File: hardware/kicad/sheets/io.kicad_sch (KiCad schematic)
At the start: 22 parts, among them J10 AUX, J11 INPUTS, Q2 AO3400A, U6 ULN2003A

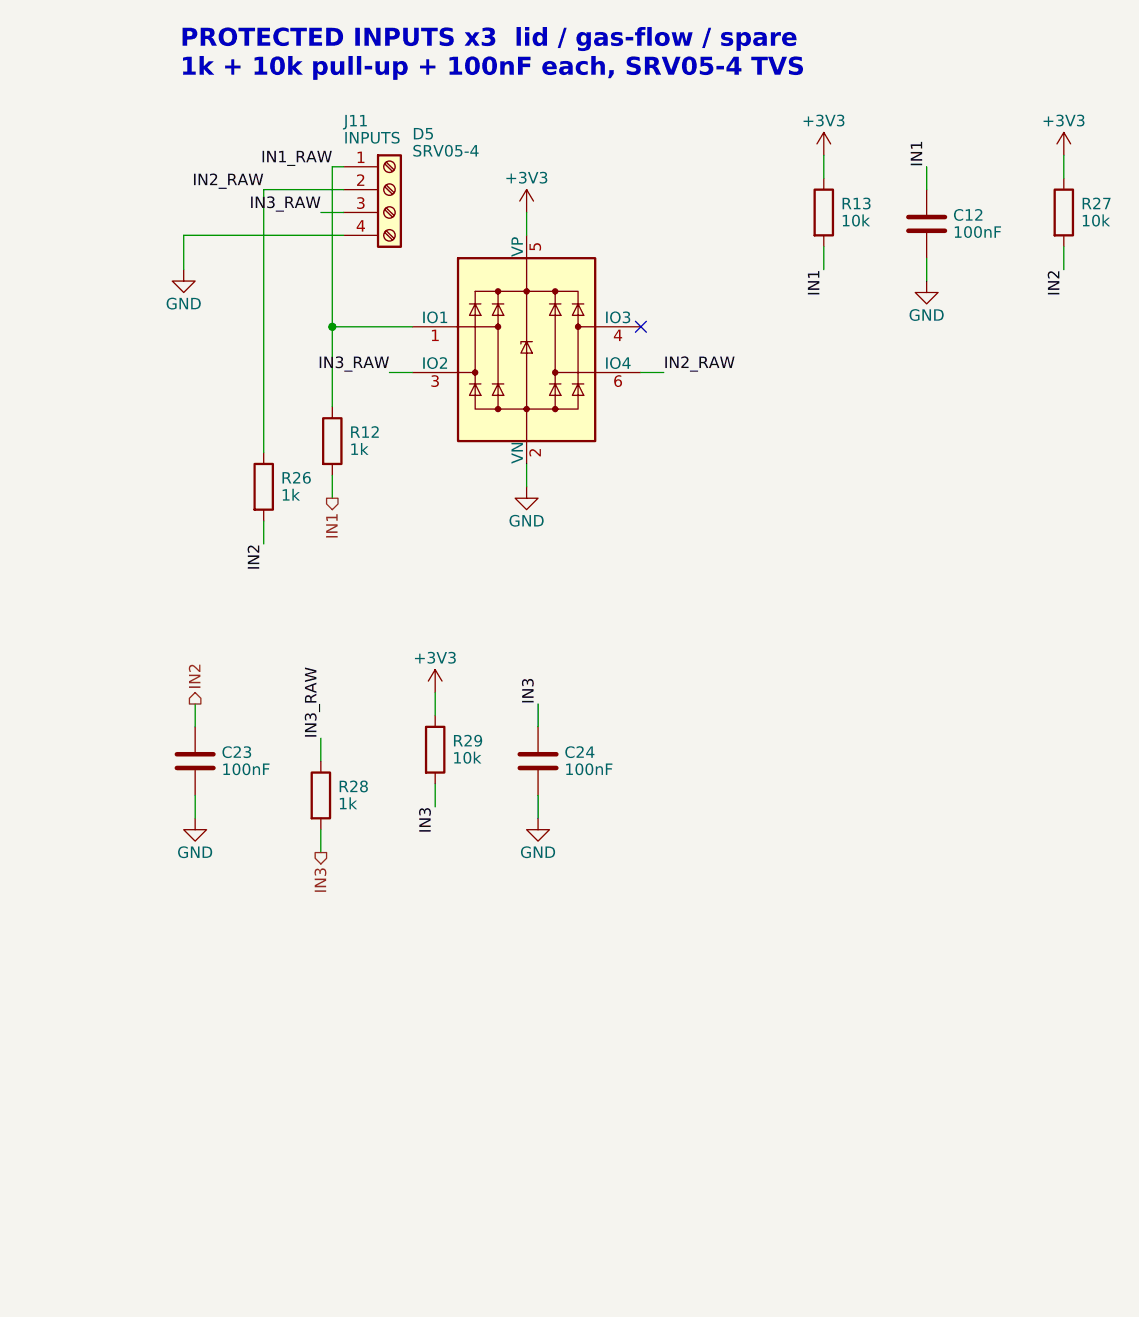
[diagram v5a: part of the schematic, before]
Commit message: hardware: inline front-ends and decoupling at the pins (review 12, 13)
Fourth batch from SCHEMATIC-REVIEW-2026-10-22.md.

Thermocouples: each MAX31856 front-end is an inline chain - the terminal
mirrored so its pins face the IC, K+ and K- on two lines through their
100R, the 100 nF differential cap bridging the lines, the 10 nF caps to
GND off each line, BIAS returned to the raw K- node along the bottom -
and AVDD/DVDD rise to a short +3V3 rail with both 100 nF hanging from
it. The ICs slid 7.62 mm right to make room; nothing else moved.

CT: J12 feeds four lines at 17.78 mm pitch with the 5R1 burden between
each pair, the 1k series parts in the path, the 33 nF to GND off each
filtered node and the 1k references off the N lines; the filtered nodes
end in the CTA_F / CTA_FN / CTB_F labels the ADE7953 pins already
carried. D6 keeps a label-fed clamp block beside the chain. VDD, VINTD
and VINTA each get a rail at the IC's top pin with their two caps on it;
R37/R38 moved 7.62 mm right to clear them.

io: IN1-IN3 are three identical rows - J11 mirrored, 1k in the path, the
10k pull-up above and 100 nF below the node, the hierarchical label at
the end - with D5's clamp block below them.

mcu: C6/C7 hang from U1's 3V3 pin. power: U2 is drawn as an inline
5 V -> 3.3 V chain with C1/C2 on its input and C3/C4 on its output in
the row the caps already occupied; LED2/R9 slid right.

Every pin landed on wiring by construction (the geometry helper checks
each symbol's pins against the wires), ERC is clean, the layout checker
reports no overlaps, the netlist still has 108 nets and the board sync
re-netted nothing. Fab outputs regenerated (schematic PDF, timestamps).

Co-Authored-By: Claude Fable 5.1 <noreply@anthropic.com>
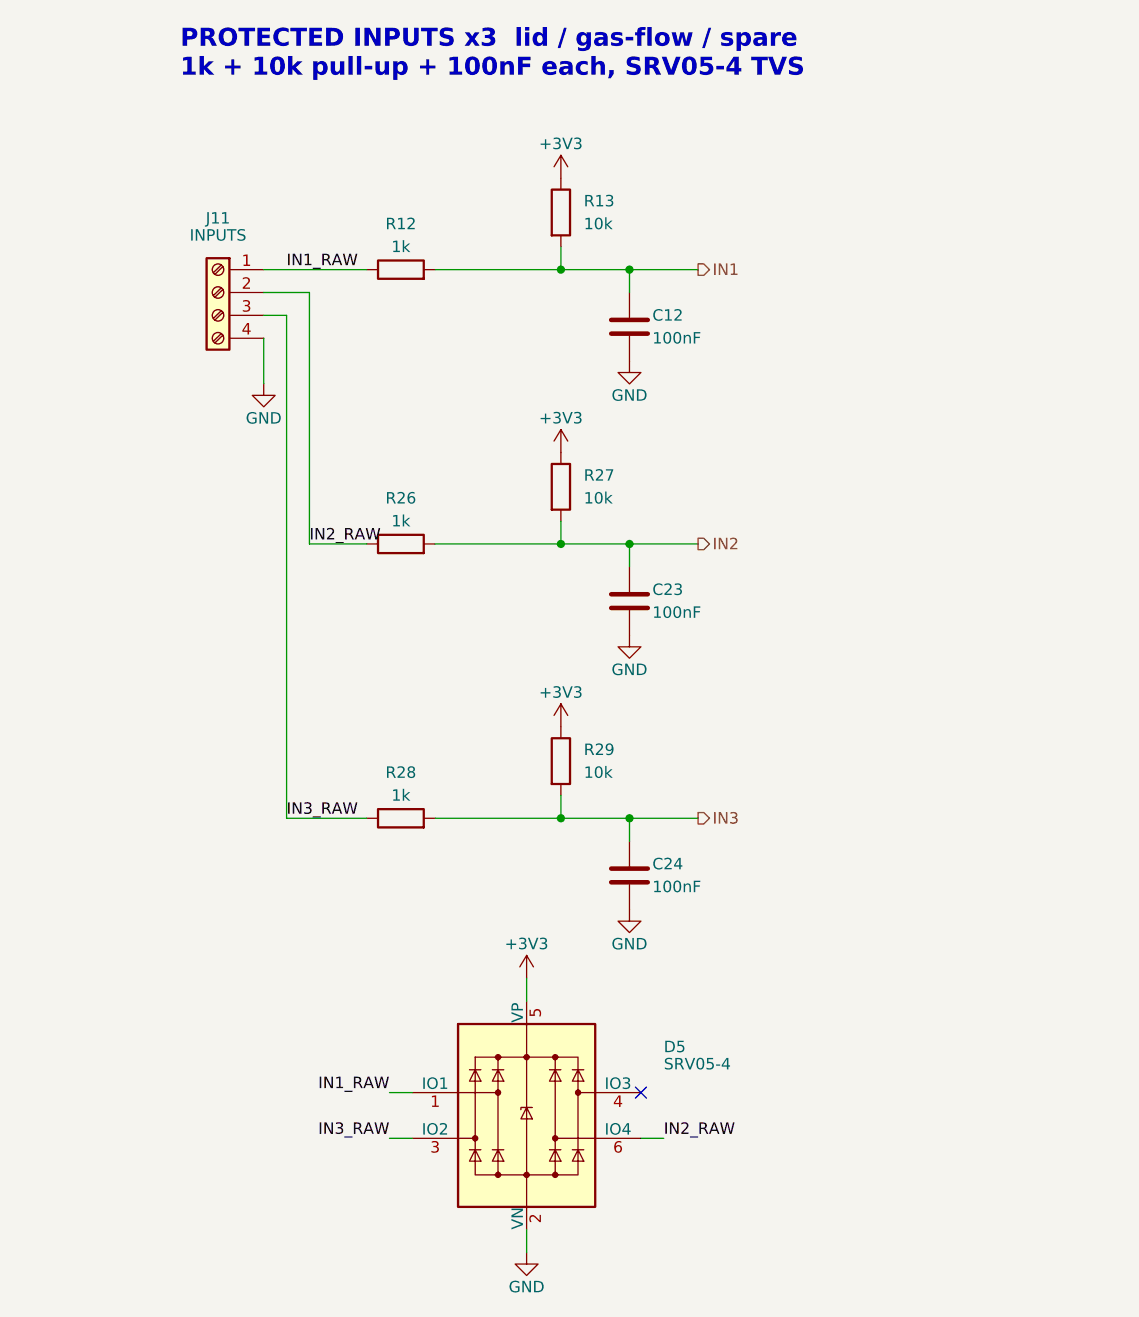
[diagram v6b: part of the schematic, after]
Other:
- moved on the sheet: C12, C23, C24, D5, J11, R12, R13, R26, R27, R28, R29

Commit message: hardware: BOM from the schematic, JLCPCB fits every part
BOM.csv is now kicad-cli's export of the schematic itself (make pcb-fab),
so every symbol not marked "Exclude from BOM" is on it; gen_jlc reads the
same flags instead of a hand-kept NOT_ASSEMBLED/HAND_SOLDER table.

JLCPCB assembly of the 12 through-hole parts plus LED1 costs ~$22 an order
against ~$110 for partial assembly and a Mouser order, so they are no
longer hand-fitted. Their Assembly field reads "Optional hand solder - JLC
assembles; untick at JLC to fit by hand"; setting it back to "HAND SOLDER"
makes a part hand-fitted again. JLC_PLACEMENT gains fitted corrections for
the six new LCSC parts (J7 needs 180 deg).

LED1 moves to the in-stock WS2812B-V5/W (C2874885): same pinout, and its
VIH of 0.63*VDD (~2.6 V at VLED) is below the old part's 2.7 V.
mouser-order.csv now holds only the mating housings and crimps.

Co-Authored-By: Claude Opus 5.5 <noreply@anthropic.com>
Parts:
- BZ1, J10, J11: Assembly (none) -> Optional hand solder - JLC assembles; untick at JLC to fit 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
- SJ1: now left out of the parts list
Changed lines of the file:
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@@
 			)
 		)
-	)
+		(property "Assembly" "Optional hand solder - JLC assembles; untick at JLC to fit by hand"
+			(at 78.74 48.26 0)
+			(hide yes)
+			(effects
+				(font
+					(size 1.27 1.27)
+				)
+			)
+		))
 	(symbol
 		(lib_id "power:+3V3")
@@
 		(body_style 1)
 		(exclude_from_sim no)
-		(in_bom yes)
+		(in_bom no)
 		(on_board yes)
 		(in_pos_files yes)
@@
 			)
 		)
-	)
+		(property "Assembly" "Optional hand solder - JLC assembles; untick at JLC to fit by hand"
+			(at 185.42 46.99 0)
+			(hide yes)
+			(effects
+				(font
+					(size 1.27 1.27)
+				)
+			)
+		))
 	(symbol
 		(lib_id "Device:R")
@@
 			)
 		)
-	)
+		(property "Assembly" "Optional hand solder - JLC assembles; untick at JLC to fit by hand"
+			(at 276.86 55.88 0)
+			(hide yes)
+			(effects
+				(font
+					(size 1.27 1.27)
+				)
+			)
+		))
 	(symbol
 		(lib_id "power:GND")
